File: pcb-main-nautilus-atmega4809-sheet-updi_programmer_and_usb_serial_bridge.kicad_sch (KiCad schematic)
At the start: 7 parts, among them U3 ATSAMD11D14A-SS

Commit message: Add nettie footprint
Supports #2.
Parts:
- NT1: footprint (none) -> NetTie:NetTie-3_SMD_Pad0.5mm
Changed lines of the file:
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@@
       (effects (font (size 1.27 1.27)) hide)
     )
-    (property "Footprint" "" (id 2) (at 167.64 101.6 0)
+    (property "Footprint" "NetTie:NetTie-3_SMD_Pad0.5mm" (id 2) (at 167.64 101.6 0)
       (effects (font (size 1.27 1.27)) hide)
     )

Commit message: Remove nettie from BOM
Supports #2.
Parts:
- NT1: now left out of the parts list
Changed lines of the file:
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@@
   )
   (symbol (lib_id "Device:NetTie_3") (at 167.64 101.6 0) (unit 1)
-    (in_bom yes) (on_board yes) (fields_autoplaced)
+    (in_bom no) (on_board yes) (fields_autoplaced)
     (property "Reference" "NT1" (id 0) (at 167.64 96.52 0)
       (effects (font (size 1.27 1.27)) hide)

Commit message: Replace Digi-Key part numbers with links
Supports #2.
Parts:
- C7: Digi-Key (none) -> https://www.digikey.com/en/products/detail/kemet/C0603C475M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; Digi-Key Part Number 399-C0603C475M8PAC7867CT-ND -> (none)
- C8, C9: Digi-Key (none) -> https://www.digikey.com/en/products/detail/kemet/C0603C104M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; Digi-Key Part Number 399-C0603C104M8RAC7867CT-ND -> (none)
- R3, R4: Digi-Key (none) -> https://www.digikey.com/en/products/detail/panasonic-electr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; Digi-Key Part Number P4.70KHCT-ND -> (none)
- U3: Digi-Key (none) -> https://www.digikey.com/en/products/detail/microchip-techno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; Digi-Key Part Number ATSAMD11D14A-SSUTCT-ND -> (none)
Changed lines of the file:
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@@
       (effects (font (size 1.27 1.27)) hide)
     )
-    (property "Digi-Key Part Number" "399-C0603C104M8RAC7867CT-ND" (id 6) (at 95.25 83.82 0)
+    (property "Digi-Key" "https://www.digikey.com/en/products/detail/kemet/C0603C104M8RAC7867/2199783" (id 6) (at 95.25 83.82 0)
       (effects (font (size 1.27 1.27)) hide)
     )
@@
       (effects (font (size 1.27 1.27)) hide)
     )
-    (property "Digi-Key Part Number" "399-C0603C104M8RAC7867CT-ND" (id 6) (at 132.08 73.66 0)
+    (property "Digi-Key" "https://www.digikey.com/en/products/detail/kemet/C0603C104M8RAC7867/2199783" (id 6) (at 132.08 73.66 0)
       (effects (font (size 1.27 1.27)) hide)
     )
@@
       (effects (font (size 1.27 1.27)) hide)
     )
-    (property "Digi-Key Part Number" "ATSAMD11D14A-SSUTCT-ND" (id 6) (at 139.7 101.6 0)
+    (property "Digi-Key" "https://www.digikey.com/en/products/detail/microchip-technology/ATSAMD11D14A-SSUT/5226474" (id 6) (at 139.7 101.6 0)
       (effects (font (size 1.27 1.27)) hide)
     )
@@
       (effects (font (size 1.27 1.27)) hide)
     )
-    (property "Digi-Key Part Number" "P4.70KHCT-ND" (id 6) (at 109.22 73.66 0)
+    (property "Digi-Key" "https://www.digikey.com/en/products/detail/panasonic-electronic-components/ERJ-3EKF4701V/1746419" (id 6) (at 109.22 73.66 0)
       (effects (font (size 1.27 1.27)) hide)
     )
@@
       (effects (font (size 1.27 1.27)) hide)
     )
-    (property "Digi-Key Part Number" "399-C0603C475M8PAC7867CT-ND" (id 6) (at 132.08 63.5 0)
+    (property "Digi-Key" "https://www.digikey.com/en/products/detail/kemet/C0603C475M8PAC7867/2200892" (id 6) (at 132.08 63.5 0)
       (effects (font (size 1.27 1.27)) hide)
     )
@@
       (effects (font (size 1.27 1.27)) hide)
     )
-    (property "Digi-Key Part Number" "P4.70KHCT-ND" (id 6) (at 78.74 91.44 0)
+    (property "Digi-Key" "https://www.digikey.com/en/products/detail/panasonic-electronic-components/ERJ-3EKF4701V/1746419" (id 6) (at 78.74 91.44 0)
       (effects (font (size 1.27 1.27)) hide)
     )

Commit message: Replace Mouser part numbers with links
Supports #2.
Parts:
- C7: Mouser (none) -> https://www.mouser.com/ProductDetail/KEMET/C0603C106M9PAC?q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; Mouser Part Number 80-C0603C475M8P -> (none)
- C8, C9: Mouser (none) -> https://www.mouser.com/ProductDetail/KEMET/C0603C104M8RACTU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; Mouser Part Number 80-C0603C104M8R -> (none)
- R3, R4: Mouser (none) -> https://www.mouser.com/ProductDetail/Panasonic/ERJ-3EKF4701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; Mouser Part Number 667-ERJ-3EKF4701V -> (none)
- U3: Mouser (none) -> https://www.mouser.com/ProductDetail/Microchip-Technology/A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; Mouser Part Number 556-ATSAMD11D14ASSUT -> (none)
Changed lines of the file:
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@@
       (effects (font (size 1.27 1.27)) hide)
     )
-    (property "Mouser Part Number" "80-C0603C104M8R" (id 7) (at 95.25 83.82 0)
+    (property "Mouser" "https://www.mouser.com/ProductDetail/KEMET/C0603C104M8RACTU?qs=t9q%2F2xDdjt%252BO6KYorkYlEw%3D%3D" (id 7) (at 95.25 83.82 0)
       (effects (font (size 1.27 1.27)) hide)
     )
@@
       (effects (font (size 1.27 1.27)) hide)
     )
-    (property "Mouser Part Number" "80-C0603C104M8R" (id 7) (at 132.08 73.66 0)
+    (property "Mouser" "https://www.mouser.com/ProductDetail/KEMET/C0603C104M8RACTU?qs=t9q%2F2xDdjt%252BO6KYorkYlEw%3D%3D" (id 7) (at 132.08 73.66 0)
       (effects (font (size 1.27 1.27)) hide)
     )
@@
       (effects (font (size 1.27 1.27)) hide)
     )
-    (property "Mouser Part Number" "556-ATSAMD11D14ASSUT" (id 7) (at 139.7 101.6 0)
+    (property "Mouser" "https://www.mouser.com/ProductDetail/Microchip-Technology/ATSAMD11D14A-SSUT?qs=lrqjml%252Bjt8f8EFewxXrzCw%3D%3D" (id 7) (at 139.7 101.6 0)
       (effects (font (size 1.27 1.27)) hide)
     )
@@
       (effects (font (size 1.27 1.27)) hide)
     )
-    (property "Mouser Part Number" "667-ERJ-3EKF4701V" (id 7) (at 109.22 73.66 0)
+    (property "Mouser" "https://www.mouser.com/ProductDetail/Panasonic/ERJ-3EKF4701V?qs=MVjVSMjNRMouVvwnqrpO2w%3D%3D" (id 7) (at 109.22 73.66 0)
       (effects (font (size 1.27 1.27)) hide)
     )
@@
       (effects (font (size 1.27 1.27)) hide)
     )
-    (property "Mouser Part Number" "80-C0603C475M8P" (id 7) (at 132.08 63.5 0)
+    (property "Mouser" "https://www.mouser.com/ProductDetail/KEMET/C0603C106M9PAC?qs=vnwGVgFuQibgQzzOtLArWQ%3D%3D" (id 7) (at 132.08 63.5 0)
       (effects (font (size 1.27 1.27)) hide)
     )
@@
       (effects (font (size 1.27 1.27)) hide)
     )
-    (property "Mouser Part Number" "667-ERJ-3EKF4701V" (id 7) (at 78.74 91.44 0)
+    (property "Mouser" "https://www.mouser.com/ProductDetail/Panasonic/ERJ-3EKF4701V?qs=MVjVSMjNRMouVvwnqrpO2w%3D%3D" (id 7) (at 78.74 91.44 0)
       (effects (font (size 1.27 1.27)) hide)
     )

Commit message: Fix manufacturer name
Supports #2.
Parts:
- U3: Manufacturer Microchip -> Microchip Technology
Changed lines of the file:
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@@
       (effects (font (size 1.27 1.27)) hide)
     )
-    (property "Manufacturer" "Microchip" (id 4) (at 139.7 101.6 0)
+    (property "Manufacturer" "Microchip Technology" (id 4) (at 139.7 101.6 0)
       (effects (font (size 1.27 1.27)) hide)
     )

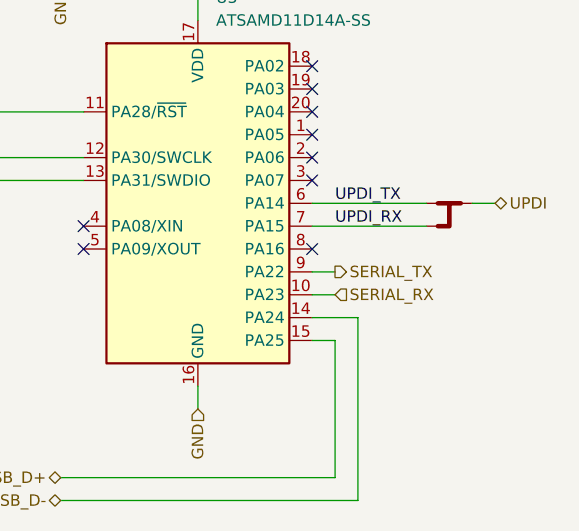
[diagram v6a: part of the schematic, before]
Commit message: Add MCU sheet
Supports #2.
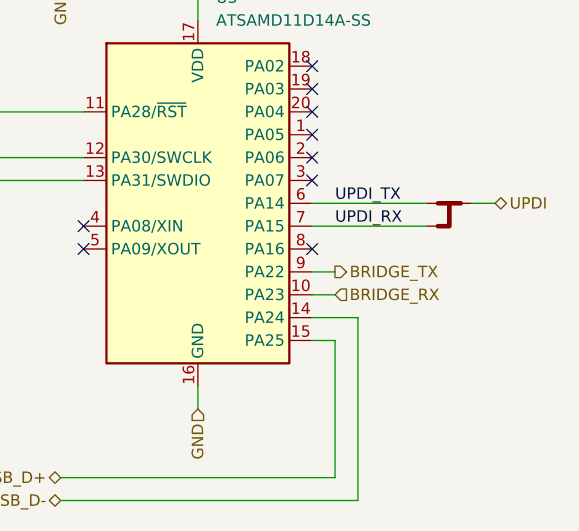
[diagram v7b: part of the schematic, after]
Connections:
- net SERIAL_RX renamed BRIDGE_RX
- net SERIAL_TX renamed BRIDGE_TX
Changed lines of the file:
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@@
     (effects (font (size 1.27 1.27)) (justify right))
   )
-  (hierarchical_label "SERIAL_TX" (shape output) (at 154.94 109.22 0)
+  (hierarchical_label "BRIDGE_TX" (shape output) (at 154.94 109.22 0)
     (effects (font (size 1.27 1.27)) (justify left))
   )
-  (hierarchical_label "SERIAL_RX" (shape input) (at 154.94 111.76 0)
+  (hierarchical_label "BRIDGE_RX" (shape input) (at 154.94 111.76 0)
     (effects (font (size 1.27 1.27)) (justify left))
   )

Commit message: Switch to generated Digi-Key and Mouser links
Supports #2.
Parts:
- C7: Digi-Key https://www.digikey.com/en/products/detail/kemet/C0603C475M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 -> (none); Digi-Key Part Number (none) -> 399-C0603C475M8PAC7867CT-ND; Mouser https://www.mouser.com/ProductDetail/KEMET/C0603C106M9PAC?q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 -> (none); Mouser Part Number (none) -> 80-C0603C106M9PAC
- C8, C9: Digi-Key https://www.digikey.com/en/products/detail/kemet/C0603C104M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 -> (none); Digi-Key Part Number (none) -> 399-C0603C104M8RAC7867CT-ND; Mouser https://www.mouser.com/ProductDetail/KEMET/C0603C104M8RACTU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 -> (none); Mouser Part Number (none) -> 80-C0603C104M8R
- R3, R4: Digi-Key https://www.digikey.com/en/products/detail/panasonic-electr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 -> (none); Digi-Key Part Number (none) -> P4.70KHCT-ND; Mouser https://www.mouser.com/ProductDetail/Panasonic/ERJ-3EKF4701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 -> (none); Mouser Part Number (none) -> 667-ERJ-3EKF4701V
- U3: Digi-Key https://www.digikey.com/en/products/detail/microchip-techno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 -> (none); Digi-Key Part Number (none) -> ATSAMD11D14A-SSUTCT-ND; Mouser https://www.mouser.com/ProductDetail/Microchip-Technology/A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 -> (none); Mouser Part Number (none) -> 556-ATSAMD11D14ASSUT
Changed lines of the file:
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@@
       (effects (font (size 1.27 1.27)) hide)
     )
-    (property "Digi-Key" "https://www.digikey.com/en/products/detail/kemet/C0603C104M8RAC7867/2199783" (id 6) (at 95.25 83.82 0)
+    (property "Digi-Key Part Number" "399-C0603C104M8RAC7867CT-ND" (id 6) (at 95.25 83.82 0)
       (effects (font (size 1.27 1.27)) hide)
     )
-    (property "Mouser" "https://www.mouser.com/ProductDetail/KEMET/C0603C104M8RACTU?qs=t9q%2F2xDdjt%252BO6KYorkYlEw%3D%3D" (id 7) (at 95.25 83.82 0)
+    (property "Mouser Part Number" "80-C0603C104M8R" (id 7) (at 95.25 83.82 0)
       (effects (font (size 1.27 1.27)) hide)
     )
@@
       (effects (font (size 1.27 1.27)) hide)
     )
-    (property "Digi-Key" "https://www.digikey.com/en/products/detail/kemet/C0603C104M8RAC7867/2199783" (id 6) (at 132.08 73.66 0)
+    (property "Digi-Key Part Number" "399-C0603C104M8RAC7867CT-ND" (id 6) (at 132.08 73.66 0)
       (effects (font (size 1.27 1.27)) hide)
     )
-    (property "Mouser" "https://www.mouser.com/ProductDetail/KEMET/C0603C104M8RACTU?qs=t9q%2F2xDdjt%252BO6KYorkYlEw%3D%3D" (id 7) (at 132.08 73.66 0)
+    (property "Mouser Part Number" "80-C0603C104M8R" (id 7) (at 132.08 73.66 0)
       (effects (font (size 1.27 1.27)) hide)
     )
@@
       (effects (font (size 1.27 1.27)) hide)
     )
-    (property "Digi-Key" "https://www.digikey.com/en/products/detail/microchip-technology/ATSAMD11D14A-SSUT/5226474" (id 6) (at 139.7 101.6 0)
+    (property "Digi-Key Part Number" "ATSAMD11D14A-SSUTCT-ND" (id 6) (at 139.7 101.6 0)
       (effects (font (size 1.27 1.27)) hide)
     )
-    (property "Mouser" "https://www.mouser.com/ProductDetail/Microchip-Technology/ATSAMD11D14A-SSUT?qs=lrqjml%252Bjt8f8EFewxXrzCw%3D%3D" (id 7) (at 139.7 101.6 0)
+    (property "Mouser Part Number" "556-ATSAMD11D14ASSUT" (id 7) (at 139.7 101.6 0)
       (effects (font (size 1.27 1.27)) hide)
     )
@@
       (effects (font (size 1.27 1.27)) hide)
     )
-    (property "Digi-Key" "https://www.digikey.com/en/products/detail/panasonic-electronic-components/ERJ-3EKF4701V/1746419" (id 6) (at 109.22 73.66 0)
+    (property "Digi-Key Part Number" "P4.70KHCT-ND" (id 6) (at 109.22 73.66 0)
       (effects (font (size 1.27 1.27)) hide)
     )
-    (property "Mouser" "https://www.mouser.com/ProductDetail/Panasonic/ERJ-3EKF4701V?qs=MVjVSMjNRMouVvwnqrpO2w%3D%3D" (id 7) (at 109.22 73.66 0)
+    (property "Mouser Part Number" "667-ERJ-3EKF4701V" (id 7) (at 109.22 73.66 0)
       (effects (font (size 1.27 1.27)) hide)
     )
@@
       (effects (font (size 1.27 1.27)) hide)
     )
-    (property "Digi-Key" "https://www.digikey.com/en/products/detail/kemet/C0603C475M8PAC7867/2200892" (id 6) (at 132.08 63.5 0)
+    (property "Digi-Key Part Number" "399-C0603C475M8PAC7867CT-ND" (id 6) (at 132.08 63.5 0)
       (effects (font (size 1.27 1.27)) hide)
     )
-    (property "Mouser" "https://www.mouser.com/ProductDetail/KEMET/C0603C106M9PAC?qs=vnwGVgFuQibgQzzOtLArWQ%3D%3D" (id 7) (at 132.08 63.5 0)
+    (property "Mouser Part Number" "80-C0603C106M9PAC" (id 7) (at 132.08 63.5 0)
       (effects (font (size 1.27 1.27)) hide)
     )
@@
       (effects (font (size 1.27 1.27)) hide)
     )
-    (property "Digi-Key" "https://www.digikey.com/en/products/detail/panasonic-electronic-components/ERJ-3EKF4701V/1746419" (id 6) (at 78.74 91.44 0)
+    (property "Digi-Key Part Number" "P4.70KHCT-ND" (id 6) (at 78.74 91.44 0)
       (effects (font (size 1.27 1.27)) hide)
     )
-    (property "Mouser" "https://www.mouser.com/ProductDetail/Panasonic/ERJ-3EKF4701V?qs=MVjVSMjNRMouVvwnqrpO2w%3D%3D" (id 7) (at 78.74 91.44 0)
+    (property "Mouser Part Number" "667-ERJ-3EKF4701V" (id 7) (at 78.74 91.44 0)
       (effects (font (size 1.27 1.27)) hide)
     )
